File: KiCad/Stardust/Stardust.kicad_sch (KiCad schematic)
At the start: 9 parts, among them IC1 TS1117BCW50_RPG, J1 Jack-DC, U1 ESP32-DEVKITC, U2 TMC2209_SILENTSTEPSTICK, U3 TMC2209_SILENTSTEPSTICK, U4 WEMOS_D1_mini, U5 RTC 3013, U6 MC7812BDTRKG, U7 56200001009

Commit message: More work on sch and board layout
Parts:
- added J2: 85513-5002, Stardust:RJ12_855135114, symbol RJ12:85513-5002
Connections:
- net at J1.1: now also U7.1
- net GND: now reaches J1.2
- net GND: now also IC1.1 (FIXED), U6.2 (GROUND)
- net at IC1.3 (INPUT): now also U6.1 (INPUT), U7.2
- net +5V: now reaches IC1.4 (OUTPUT_2)
- net +12V: now reaches U6.3 (OUTPUT)
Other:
- note added: "Power Input and Cond"
- moved on the sheet: IC1, J1, U1, U4, U5, U6, U7

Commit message: Finished schematic (V1.0)
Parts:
- removed U5: RTC 3013, Stardust:MODULE_3013, symbol RTC:3013
- removed U6: MC7812BDTRKG, Stardust:12VREG_DPAK-3_ONS, symbol 12V Regulator:MC7812BDTRKG
- added C1, C2: 10 uF, symbol Device:C_Polarized_Small_US
- added C10, C4, C5, C6: 100nF, symbol Device:C_Small
- added C3: 10uF, symbol Device:C_Small
- added C7: 100 uF, symbol Device:C_Polarized_Small_US
- added C9: 330nF, symbol Device:C_Small
- added D1: PWR LED, symbol Device:LED
- added D2: STATUS LED, symbol Device:LED
- added J3, J7: 1x2 Connector, Connector_PinHeader_2.54mm:PinHeader_1x02_P2.54mm_Vertical, symbol Connector:Conn_01x02_Pin
- added J4, J5: Conn_01x04_Pin, symbol Connector:Conn_01x04_Pin
- added J6: 1x3 Header, symbol Connector:Conn_01x03_Pin
- added J8: Conn_01x19_Pin, symbol Connector:Conn_01x19_Pin
- added R1, R10, R3, R4, R5, R6, R7, R8, R9: 4.7K, Resistor_SMD:R_0402_1005Metric, symbol Device:R_Small_US
- added R11, R12, R13, R14, R15: 2.4K, Resistor_SMD:R_0402_1005Metric, symbol Device:R_Small_US
- added R2: 1K, Resistor_SMD:R_0402_1005Metric, symbol Device:R_Small_US
- J1: value Jack-DC -> 12V DC
- J2: value 85513-5002 -> RJ12
- U1: value ESP32-DEVKITC -> ESP32; Availability Not in stock -> (none); Check_prices https://www.snapeda.com/parts/ESP32-DEVKITC/Espressif+Syste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 -> (none); Description_1 ESP32-WROOM-32UE series Transceiver; 802.11 b/g/n (Wi-Fi, W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 -> (none); Link (none) -> https://www.digikey.com/en/products/detail/espressif-system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; MANUFACTURER ESPRESSIF -> (none); MP ESP32-DEVKITC -> (none); PARTREV N/A -> (none); Package None -> (none); Price None -> (none); STANDARD Manufacturer Recommendations -> (none); SnapEDA_Link https://www.snapeda.com/parts/ESP32-DEVKITC/Espressif+Syste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 -> (none)
- U2, U3: value TMC2209_SILENTSTEPSTICK -> BTT TMC2209 V1.3; Availability Not in stock -> (none); Check_prices https://www.snapeda.com/parts/TMC2209%20SILENTSTEPSTICK/Tri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 -> (none); Description_1 TMC2209 Motor Controller/Driver Power Management Evaluation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 -> (none); MANUFACTURER Trinamic Motion Control GmbH -> (none); MF Trinamic Motion Control GmbH -> BIGTREETECH; MP TMC2209 SILENTSTEPSTICK -> (none); PARTREV 1.20 -> (none); Package None -> (none); Price None -> (none); SNAPEDA_PN TMC2209 SILENTSTEPSTICK -> (none); STANDARD Manufacturer Recommendations -> (none); SnapEDA_Link https://www.snapeda.com/parts/TMC2209%20SILENTSTEPSTICK/Tri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 -> (none)
- U7: renamed from IC1; value TS1117BCW50_RPG -> Regulator - 5V 1A
- U8: renamed from U7; value 56200001009 -> LittlFuse 2.5 Amp
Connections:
- net +12V: now also U2.16 (VM), U3.16 (VM), U7.3 (INPUT), C10.1, C2.1, C7.1, J3.2 (Pin_2)
- net +5V: now also U1.19 (EXT_5V), U4.9 (5V), C1.1, C9.1, D1.2 (A), J7.1 (Pin_1), J8.2 (Pin_2)
- net GND: now also J2.5, U1.14 (GND1), U1.32 (GND2), U1.38 (GND3), U2.15 (GND), U2.2 (MS1), U2.3 (MS2), U2.9 (GND), U3.15 (GND), U3.2 (MS1), U3.9 (GND), U4.10 (GND), C1.2, C10.2, C2.2, C3.1, C4.1, C5.1, C6.1, C7.2, C9.2, J8.1 (Pin_1), R10.2, R9.2
- net at U8.2: now also J3.1 (Pin_1); no longer U7.3 (INPUT)
- net EN: now reaches U2.1 (~{EN})
- net EN: now also U1.29 (IO5), U3.1 (~{EN}), R1.1; no longer U2.7 (GND)
- net +3.3V: now reaches U2.10 (VDD)
- net +3.3V: now also U1.1 (3V3), U3.10 (VDD), U3.3 (MS2), J8.15 (Pin_15), J8.16 (Pin_16), R1.2, R11.2, R12.2, R13.2, R14.2, R15.2, R3.2, R8.2
- net B2_1: now reaches U2.11 (B2)
- net B2_1: now also J4.1 (Pin_1)
- net B1_1: now reaches U2.12 (B1)
- net B1_1: now also J4.4 (Pin_4)
- net A1_1: now reaches U2.13 (A1)
- net A1_1: now also J4.3 (Pin_3)
- net A2_1: now reaches U2.14 (A2)
- net A2_1: now also J4.2 (Pin_2)
- net UART_RX: now reaches U2.4 (PDN)
- net UART_RX: now also U1.4 (SENSOR_VN), U3.4 (PDN), R2.2
- net DIR_1: now reaches U2.8 (DIR)
- net DIR2: now reaches U1.10 (IO26)
- net STEP2: now reaches U1.11 (IO27)
- net AUX3: now reaches U1.12 (IO14)
- net AUX3: now also C5.2, J8.7 (Pin_7)
- net STA: now reaches U1.13 (IO12)
- net STA: now also D2.2 (A)
- net AUX4: now reaches U1.15 (IO13)
- net AUX4: now also C6.2, J8.8 (Pin_8)
- net ESP32_RST: now reaches U1.2 (EN)
- net ESP32_RST: now also C3.2
- net DIR1: now reaches U1.25 (IO0)
- net UART_TX: now reaches U1.26 (IO4)
- net UART_TX: now also R2.1, R3.1
- net RX2: now reaches U1.27 (IO16)
- net RX2: now also U4.7 (CS/D8)
- net TX2: now reaches U1.28 (IO17)
- net TX2: now also U4.6 (MOSI/D7)
- net PEC: now reaches U1.3 (SENSOR_VP)
- net PEC: now also C4.2, J8.13 (Pin_13)
- net STEP1: now reaches U1.30 (IO18)
- net SDA: now reaches U1.33 (IO21)
- net SDA: now also J8.12 (Pin_12)
- net TX0: now reaches U1.34 (RXD0)
- net TX0: now also J8.9 (Pin_9)
- net RX0: now reaches U1.35 (TXD0)
- net RX0: now also J8.10 (Pin_10)
- net SCL: now reaches U1.36 (IO22)
- net SCL: now also J8.11 (Pin_11)
- net AUX7: now reaches U1.37 (IO23)
- net AUX7: now also J8.14 (Pin_14), J8.18 (Pin_18)
- net RA-: now reaches U1.5 (IO34)
- net RA-: now also J2.4, R11.1
- net RA+: now reaches U1.6 (IO35)
- net RA+: now also J2.1, R14.1
- net DE-: now reaches U1.7 (IO32)
- net DE-: now also J2.3, R12.1
- net DE+: now reaches U1.8 (IO33)
- net DE+: now also J2.2, R13.1
- net AUX8: now reaches U1.9 (IO25)
- net AUX8: now also R15.1, R8.1
- net STEP_2: now reaches U3.7 (STEP)
- net STEP_2: no longer U3.1 (GND)
- net B2_2: now reaches U3.11 (B2)
- net B2_2: now also J5.1 (Pin_1)
- net B1_2: now reaches U3.12 (B1)
- net B1_2: now also J5.4 (Pin_4)
- net A1_2: now reaches U3.13 (A1)
- net A1_2: now also J5.3 (Pin_3)
- net A2_2: now reaches U3.14 (A2)
- net A2_2: now also J5.2 (Pin_2)
- net DIR_2: now reaches U3.8 (DIR)
- net EN2_B: now reaches U4.13 (SDA/D2)
- net EN2_B: now also J8.5 (Pin_5), R6.1
- net EN2_A: now reaches U4.14 (SCL/D1)
- net EN2_A: now also J8.6 (Pin_6), R7.1
- net EN1_A: now reaches U4.4 (SCK/D5)
- net EN1_A: now also J8.4 (Pin_4), R5.1
- net EN1_B: now reaches U4.5 (MISO/D6)
- net EN1_B: now also J8.3 (Pin_3), R4.1
- net at J2.6: now also J7.2 (Pin_2)
- new net: D1.1 (K), R9.1
- new net: D2.1 (K), R10.1
- new net LIMIT: J8.17 (Pin_17)
- new net PPS: J8.19 (Pin_19)
- new net PUL: R4.2, R5.2, R6.2, R7.2
- new net STEP_1: U2.7 (STEP)
- no-connect marks 0 -> 24
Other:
- note added: "15V MAX"
- note added: "Address - 00"
- note added: "Address - 01"
- note added: "Connectors and Misc"
- note added: "Processor"
- note added: "Stepper Drivers"
- note added: "Using BTT TMC2209 V1.3 Drivers"
- note added: "WIFI"
- moved on the sheet: J2, U4, U7

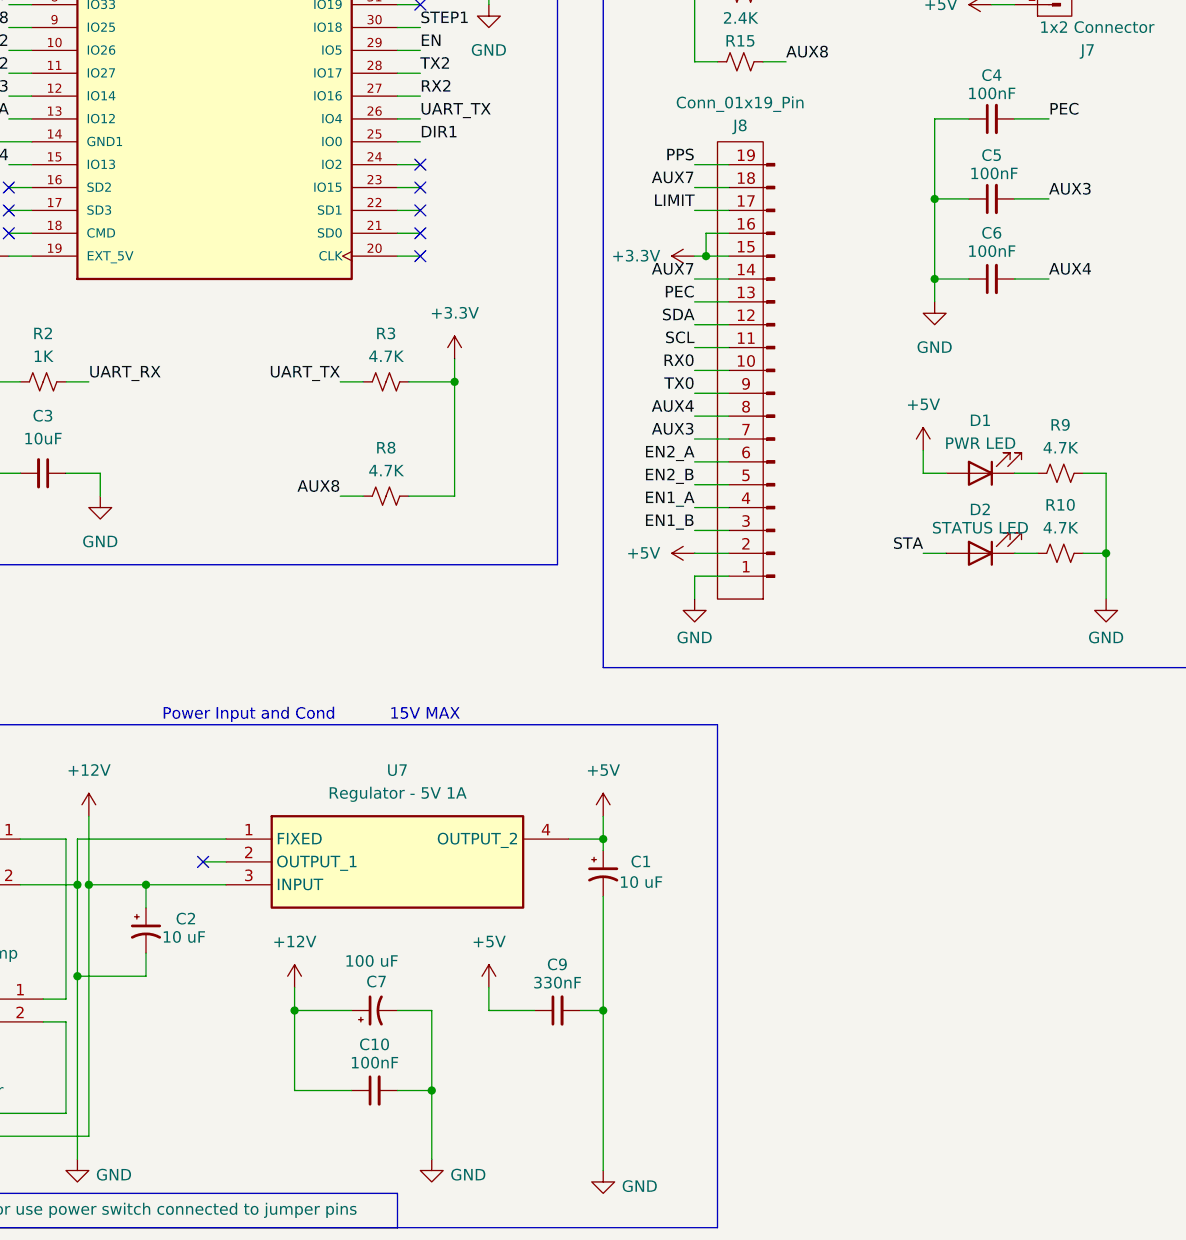
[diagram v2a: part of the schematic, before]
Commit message: Added parts for everything as well as assigned footprints. Board should be ready to finish
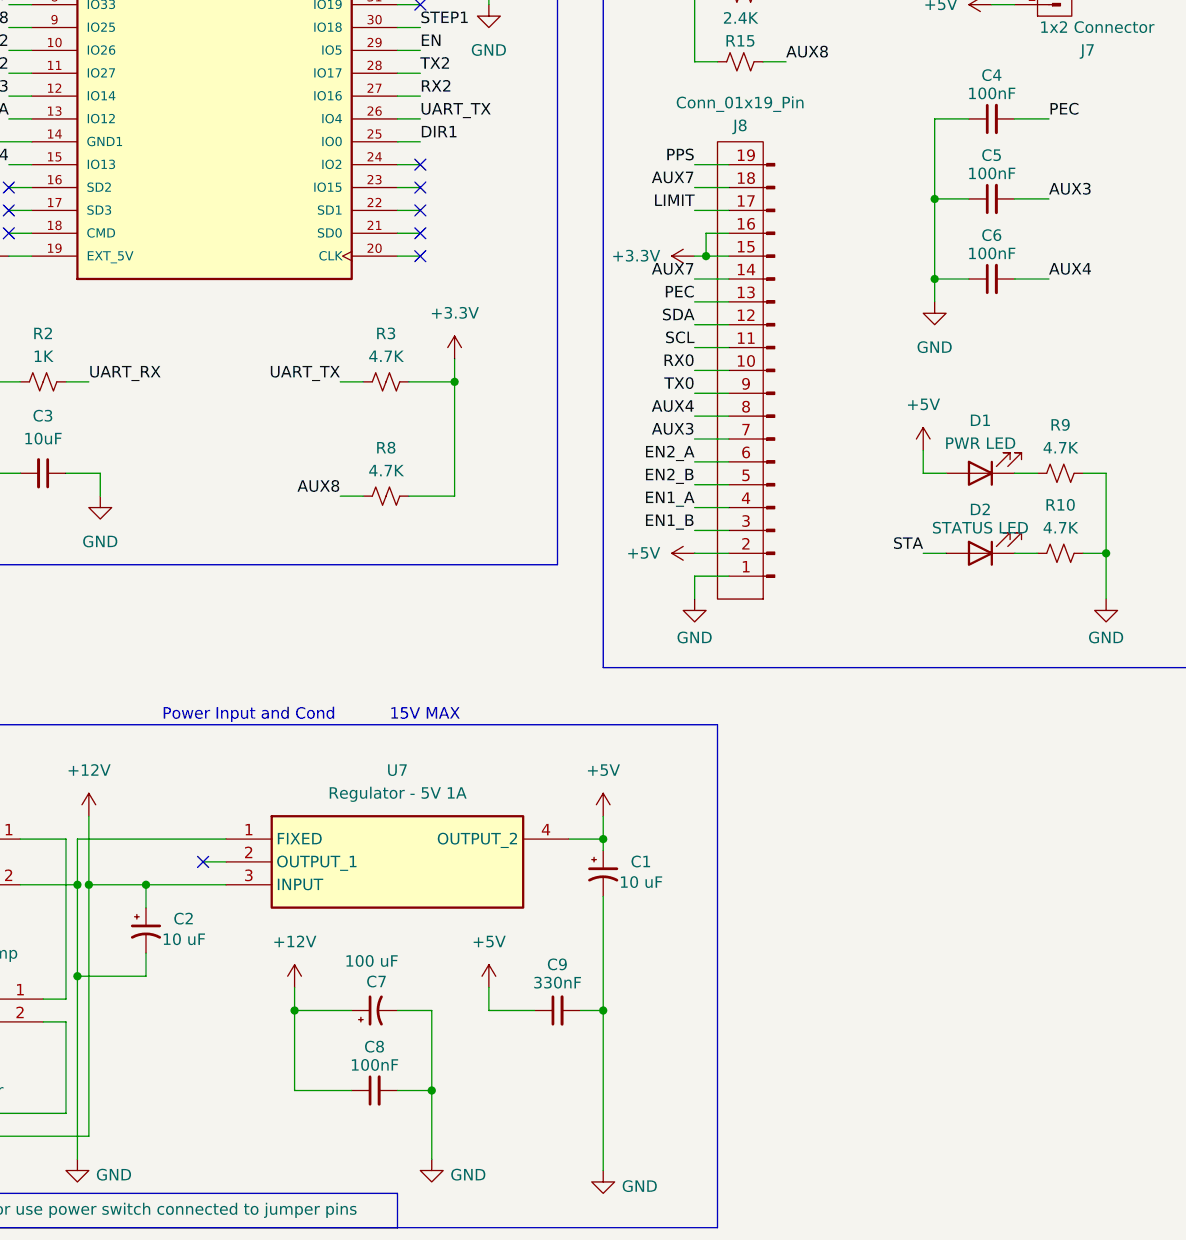
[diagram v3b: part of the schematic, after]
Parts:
- removed C10: 100nF, symbol Device:C_Small
- added C8: 100nF, Capacitor_SMD:C_2220_5750Metric_Pad1.97x5.40mm_HandSolder, symbol Device:C_Small
- C1, C2: footprint (none) -> Stardust:10uFElectrolyticCap_CAPAE660X550N; Mouser PN (none) -> 710-865230643009
- C3: footprint (none) -> Capacitor_SMD:C_0603_1608Metric_Pad1.08x0.95mm_HandSolder; Mouser PN (none) -> 810-C1608X7T1A106M08
- C4, C5, C6: footprint (none) -> Capacitor_SMD:C_2220_5750Metric_Pad1.97x5.40mm_HandSolder; Mouser PN (none) -> 810-Q1C0G2J104G280KC
- C7: footprint (none) -> Stardust:100uFElectrolyticCap_CAPAE830X1080N; Mouser PN  (none) -> 647-GXC1V101MCQ1GS
- C9: footprint (none) -> Capacitor_SMD:C_1206_3216Metric_Pad1.33x1.80mm_HandSolder; Mouser PN (none) -> 581-KAM31NR81H334KU
- D1, D2: footprint (none) -> LED_SMD:LED_0603_1608Metric_Pad1.05x0.95mm_HandSolder
- J4, J5: footprint (none) -> Connector_PinHeader_2.54mm:PinHeader_1x04_P2.54mm_Vertical
- J6: footprint (none) -> Connector_PinHeader_2.54mm:PinHeader_1x03_P2.54mm_Vertical
- J8: footprint (none) -> Connector_PinHeader_2.54mm:PinHeader_1x19_P2.54mm_Vertical
- R1, R10, R11, R12, R13, R14, R15, R2, R3, R4, R5, R6, R7, R8, R9: footprint Resistor_SMD:R_0402_1005Metric -> Resistor_SMD:R_0805_2012Metric_Pad1.20x1.40mm_HandSolder
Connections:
- net +12V: now also C8.1
- net GND: now also C8.2

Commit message: Finished board design and created gerber files
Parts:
- removed R8: 4.7K, Resistor_SMD:R_0805_2012Metric_Pad1.20x1.40mm_HandSolder, symbol Device:R_Small_US
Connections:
- net +3.3V: now also J6.3 (Pin_3)
- net GND: now also J6.1 (Pin_1)
- net PUL: now also J6.2 (Pin_2)
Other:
- moved on the sheet: J6
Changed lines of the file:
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@@
 	)
 	(junction
-		(at 86.36 95.25)
-		(diameter 0)
-		(color 0 0 0 0)
-	)
-	(junction
 		(at 114.3 81.28)
 		(diameter 0)
@@
 	(wire
 		(pts
-			(xy 81.28 107.95) (xy 86.36 107.95)
-		)
-		(stroke
-			(width 0)
-			(type default)
-		)
-	)
-	(wire
-		(pts
 			(xy 36.83 73.66) (xy 39.37 73.66)
 		)
@@
 	(wire
 		(pts
-			(xy 86.36 95.25) (xy 86.36 107.95)
-		)
-		(stroke
-			(width 0)
-			(type default)
-		)
-	)
-	(wire
-		(pts
 			(xy 90.17 35.56) (xy 90.17 38.1)
 		)
@@
 	(wire
 		(pts
-			(xy 73.66 107.95) (xy 76.2 107.95)
-		)
-		(stroke
-			(width 0)
-			(type default)
-		)
-	)
-	(wire
-		(pts
 			(xy 80.01 63.5) (xy 82.55 63.5)
 		)
@@
 		)
 	)
-	(label "AUX8"
-		(at 73.66 107.95 180)
-		(effects
-			(font
-				(size 1.27 1.27)
-			)
-			(justify right bottom)
-		)
-	)
 	(label "EN1_B"
 		(at 208.28 135.89 0)
@@
 	)
 	(symbol
-		(lib_id "Device:R_Small_US")
-		(at 78.74 107.95 90)
-		(unit 1)
-		(exclude_from_sim no)
-		(in_bom yes)
-		(on_board yes)
-		(dnp no)
-		(property "Reference" "R8"
-			(at 78.74 102.616 90)
-			(effects
-				(font
-					(size 1.27 1.27)
-				)
-			)
-		)
-		(property "Value" "4.7K"
-			(at 78.74 105.156 90)
-			(effects
-				(font
-					(size 1.27 1.27)
-				)
-			)
-		)
-		(property "Footprint" "Resistor_SMD:R_0805_2012Metric_Pad1.20x1.40mm_HandSolder"
-			(at 78.74 107.95 0)
-			(effects
-				(font
-					(size 1.27 1.27)
-				)
-				(hide yes)
-			)
-		)
-		(property "Datasheet" "~"
-			(at 78.74 107.95 0)
-			(effects
-				(font
-					(size 1.27 1.27)
-				)
-				(hide yes)
-			)
-		)
-		(property "Description" "Resistor, small US symbol"
-			(at 78.74 107.95 0)
-			(effects
-				(font
-					(size 1.27 1.27)
-				)
-				(hide yes)
-			)
-		)
-		(pin "1"
-		)
-		(pin "2"
-		)
-		(instances
-			(project "Stardust"
-				(path "/0cf7f69c-baaa-4387-8176-0e8bab43a342"
-					(reference "R8")
-					(unit 1)
-				)
-			)
-		)
-	)
-	(symbol
 		(lib_id "Device:C_Polarized_Small_US")
 		(at 77.47 165.1 90)
@@
 	(symbol
 		(lib_id "Connector:Conn_01x03_Pin")
-		(at 232.41 129.54 180)
+		(at 227.33 129.54 0)
+		(mirror x)
 		(unit 1)
 		(exclude_from_sim no)
@@
 		(dnp no)
 		(property "Reference" "J6"
-			(at 228.346 120.904 0)
+			(at 231.394 120.904 0)
 			(effects
 				(font
@@
 		)
 		(property "Value" "1x3 Header"
-			(at 228.346 123.444 0)
+			(at 231.394 123.444 0)
 			(effects
 				(font
@@
 		)
 		(property "Footprint" "Connector_PinHeader_2.54mm:PinHeader_1x03_P2.54mm_Vertical"
-			(at 232.41 129.54 0)
+			(at 227.33 129.54 0)
 			(effects
 				(font
@@
 		)
 		(property "Datasheet" "~"
-			(at 232.41 129.54 0)
+			(at 227.33 129.54 0)
 			(effects
 				(font
@@
 		)
 		(property "Description" "Generic connector, single row, 01x03, script generated"
-			(at 232.41 129.54 0)
+			(at 227.33 129.54 0)
 			(effects
 				(font

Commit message: Added silkscreen images
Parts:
- added G1: LOGO, images:logo_footprint, symbol logo_symbol:LOGO
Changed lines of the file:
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@@
+	)
+	(symbol
+		(lib_id "logo_symbol:LOGO")
+		(at 255.27 161.29 0)
+		(unit 1)
+		(exclude_from_sim no)
+		(in_bom yes)
+		(on_board yes)
+		(dnp no)
+		(fields_autoplaced yes)
+		(property "Reference" "G1"
+			(at 255.27 128.397 0)
+			(effects
+				(font
+					(size 1.27 1.27)
+				)
+				(hide yes)
+			)
+		)
+		(property "Value" "LOGO"
+			(at 255.27 194.183 0)
+			(effects
+				(font
+					(size 1.27 1.27)
+				)
+				(hide yes)
+			)
+		)
+		(property "Footprint" "images:logo_footprint"
+			(at 255.27 161.29 0)
+			(effects
+				(font
+					(size 1.27 1.27)
+				)
+			)
+		)
+		(property "Datasheet" ""
+			(at 255.27 161.29 0)
+			(effects
+				(font
+					(size 1.27 1.27)
+				)
+				(hide yes)
+			)
+		)
+		(property "Description" ""
+			(at 255.27 161.29 0)
+			(effects
+				(font
+					(size 1.27 1.27)
+				)
+				(hide yes)
+			)
+		)
+		(instances
+			(project ""
+				(path "/0cf7f69c-baaa-4387-8176-0e8bab43a342"
+					(reference "G1")
+					(unit 1)
+				)
+			)
+		)
 	)
 	(symbol
